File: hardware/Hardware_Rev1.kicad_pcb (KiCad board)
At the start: 2 copper layers, 101.6 x 50.8 mm, 52 parts, among them J1 RJ45_LED_Shielded, J2 6P6C, Q1 BUK7M33-60EX, Q2 BUK7M33-60EX, Q3 BUK7M33-60EX, U1 LT1910, U2 LT1910, U3 OKI, U4 LT1910, U5 TSR_1-2450, U6 Teensy4.1_DEV-16771

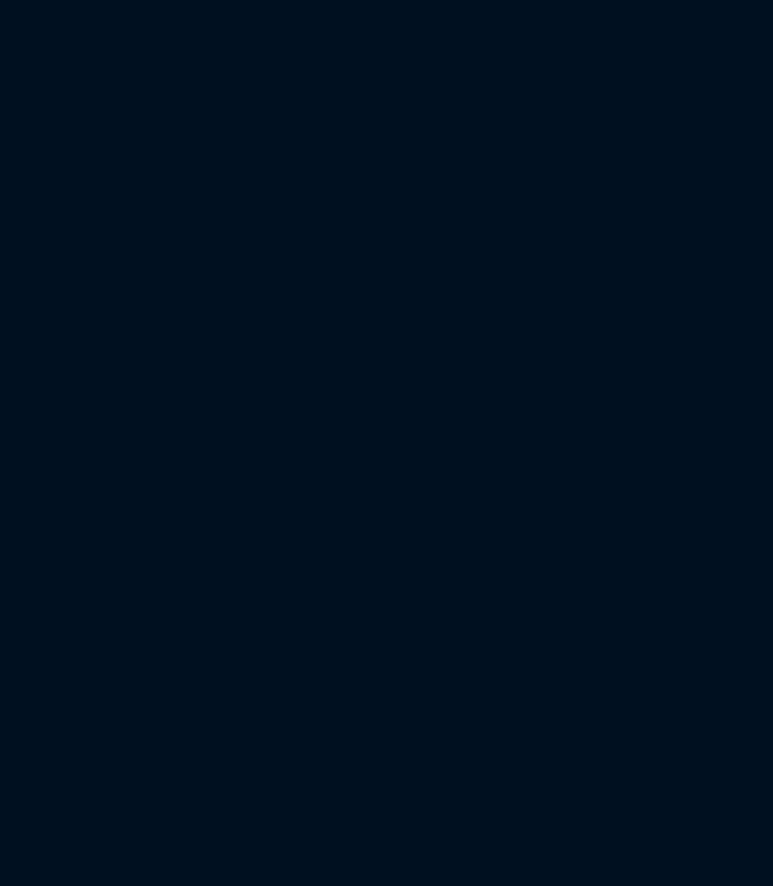
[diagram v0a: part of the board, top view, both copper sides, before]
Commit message: updated layout with drill holes (they don't fit??)
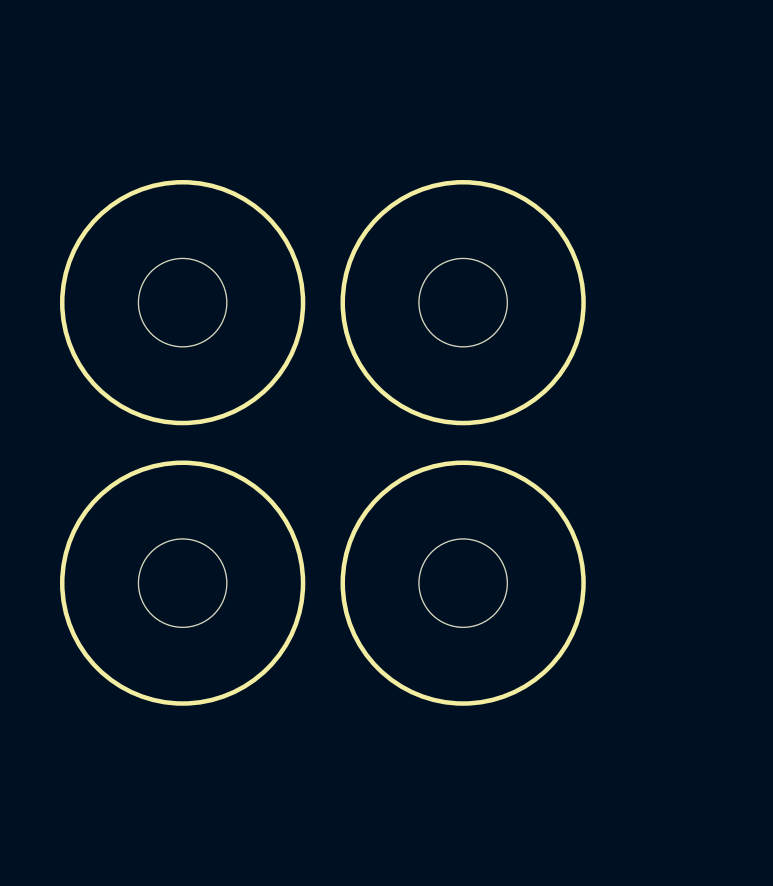
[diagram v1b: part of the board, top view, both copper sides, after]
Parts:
- added V1: Via, MRDT_Drill_Holes:4_40_Hole_Corner, F.Cu at (-342.9, -57.1)
- added V2: Via, MRDT_Drill_Holes:4_40_Hole_Corner, F.Cu at (-334.9, -66.5)
- added V3: Via, MRDT_Drill_Holes:4_40_Hole_Corner, F.Cu at (-333.6, -57.1)
- added V4: Via, MRDT_Drill_Holes:4_40_Hole_Corner, F.Cu at (-333.6, -66.5)
- Q1, Q2, Q3: value BUK7M33-60EX -> BUK9M9R5-40HX
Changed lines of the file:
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@@
     )
+  )
+  (footprint "MRDT_Drill_Holes:4_40_Hole_Corner" (layer "F.Cu")
+    (at -333.55 -57.15)
+    (property "Sheetfile" "Hardware_Rev1.kicad_sch")
+    (property "Sheetname" "")
+    (attr through_hole)
+    (fp_text reference "V3" (at 4.00812 -3.50812) (layer "F.SilkS") hide
+      (effects (font (size 1 1) (thickness 0.15)))
+    )
+    (fp_text value "Via" (at 4.00812 -4.50812) (layer "F.Fab") hide
+      (effects (font (size 1 1) (thickness 0.15)))
+    )
+    (fp_circle (center 4.00812 -4.00812) (end 4.00812 0.00508) (layer "F.SilkS") (width 0.15) (fill none))
+    (fp_line (start 4.0132 -8.0264) (end 0 -8.0264) (layer "F.Fab") (width 0.15))
+    (fp_line (start 0 0) (end 8.0264 0) (layer "F.Fab") (width 0.15))
+    (fp_line (start 8.0264 -4.0132) (end 8.0264 0) (layer "F.Fab") (width 0.15))
+    (fp_line (start 0 -8.0264) (end 0 0) (layer "F.Fab") (width 0.15))
+    (fp_arc (start 4.0132 -8.0264) (mid 6.850961 -6.850961) (end 8.0264 -4.0132) (layer "F.Fab") (width 0.15))
+    (pad "" np_thru_hole circle locked (at 4.00812 -4.00812) (size 2.9464 2.9464) (drill 2.9464) (layers *.Cu *.Mask)
+      (clearance 2.5))
   )
   (footprint "Capacitor_SMD:C_0603_1608Metric_Pad1.08x0.95mm_HandSolder" (layer "F.Cu")
@@
     )
   )
+  (footprint "MRDT_Drill_Holes:4_40_Hole_Corner" (layer "F.Cu")
+    (at -334.88376 -66.5 90)
+    (property "Sheetfile" "Hardware_Rev1.kicad_sch")
+    (property "Sheetname" "")
+    (attr through_hole)
+    (fp_text reference "V2" (at 4.00812 -3.50812 90) (layer "F.SilkS") hide
+      (effects (font (size 1 1) (thickness 0.15)))
+    )
+    (fp_text value "Via" (at 4.00812 -4.50812 90) (layer "F.Fab") hide
+      (effects (font (size 1 1) (thickness 0.15)))
+    )
+    (fp_circle (center 4.00812 -4.00812) (end 4.00812 0.00508) (layer "F.SilkS") (width 0.15) (fill none))
+    (fp_line (start 8.0264 -4.0132) (end 8.0264 0) (layer "F.Fab") (width 0.15))
+    (fp_line (start 0 0) (end 8.0264 0) (layer "F.Fab") (width 0.15))
+    (fp_line (start 4.0132 -8.0264) (end 0 -8.0264) (layer "F.Fab") (width 0.15))
+    (fp_line (start 0 -8.0264) (end 0 0) (layer "F.Fab") (width 0.15))
+    (fp_arc (start 4.0132 -8.0264) (mid 6.850961 -6.850961) (end 8.0264 -4.0132) (layer "F.Fab") (width 0.15))
+    (pad "" np_thru_hole circle locked (at 4.00812 -4.00812 90) (size 2.9464 2.9464) (drill 2.9464) (layers *.Cu *.Mask)
+      (clearance 2.5))
+  )
   (footprint "MRDT_Connectors:MOLEX_uF_S_03_Horizontal" (layer "F.Cu")
     (at -158.82 3.75 180)
@@
       (effects (font (size 1 1) (thickness 0.15)))
     )
-    (fp_text value "BUK7M33-60EX" (at 0 2.64) (layer "F.Fab")
+    (fp_text value "BUK9M9R5-40HX" (at 0 2.64) (layer "F.Fab")
       (effects (font (size 1 1) (thickness 0.15)))
     )
@@
       (effects (font (size 1 1) (thickness 0.15)))
     )
-    (fp_text value "BUK7M33-60EX" (at 0 2.64) (layer "F.Fab")
+    (fp_text value "BUK9M9R5-40HX" (at 0 2.64) (layer "F.Fab")
       (effects (font (size 1 1) (thickness 0.15)))
     )
@@
     )
   )
+  (footprint "MRDT_Drill_Holes:4_40_Hole_Corner" (layer "F.Cu")
+    (at -333.55 -66.5)
+    (property "Sheetfile" "Hardware_Rev1.kicad_sch")
+    (property "Sheetname" "")
+    (attr through_hole)
+    (fp_text reference "V4" (at 4.00812 -3.50812) (layer "F.SilkS") hide
+      (effects (font (size 1 1) (thickness 0.15)))
+    )
+    (fp_text value "Via" (at 4.00812 -4.50812) (layer "F.Fab") hide
+      (effects (font (size 1 1) (thickness 0.15)))
+    )
+    (fp_circle (center 4.00812 -4.00812) (end 4.00812 0.00508) (layer "F.SilkS") (width 0.15) (fill none))
+    (fp_line (start 0 0) (end 8.0264 0) (layer "F.Fab") (width 0.15))
+    (fp_line (start 4.0132 -8.0264) (end 0 -8.0264) (layer "F.Fab") (width 0.15))
+    (fp_line (start 8.0264 -4.0132) (end 8.0264 0) (layer "F.Fab") (width 0.15))
+    (fp_line (start 0 -8.0264) (end 0 0) (layer "F.Fab") (width 0.15))
+    (fp_arc (start 4.0132 -8.0264) (mid 6.850961 -6.850961) (end 8.0264 -4.0132) (layer "F.Fab") (width 0.15))
+    (pad "" np_thru_hole circle locked (at 4.00812 -4.00812) (size 2.9464 2.9464) (drill 2.9464) (layers *.Cu *.Mask)
+      (clearance 2.5))
+  )
   (footprint "Capacitor_SMD:C_0603_1608Metric_Pad1.08x0.95mm_HandSolder" (layer "F.Cu")
     (at -85.25 -60.59)
@@
       (effects (font (size 1 1) (thickness 0.15)))
     )
-    (fp_text value "BUK7M33-60EX" (at 0 2.64) (layer "F.Fab")
+    (fp_text value "BUK9M9R5-40HX" (at 0 2.64) (layer "F.Fab")
       (effects (font (size 1 1) (thickness 0.15)))
     )
@@
     )
   )
+  (footprint "MRDT_Drill_Holes:4_40_Hole_Corner" (layer "F.Cu")
+    (at -342.9 -57.15)
+    (property "Sheetfile" "Hardware_Rev1.kicad_sch")
+    (property "Sheetname" "")
+    (attr through_hole)
+    (fp_text reference "V1" (at 4.00812 -3.50812) (layer "F.SilkS") hide
+      (effects (font (size 1 1) (thickness 0.15)))
+    )
+    (fp_text value "Via" (at 4.00812 -4.50812) (layer "F.Fab") hide
+      (effects (font (size 1 1) (thickness 0.15)))
+    )
+    (fp_circle (center 4.00812 -4.00812) (end 4.00812 0.00508) (layer "F.SilkS") (width 0.15) (fill none))
+    (fp_line (start 0 -8.0264) (end 0 0) (layer "F.Fab") (width 0.15))
+    (fp_line (start 4.0132 -8.0264) (end 0 -8.0264) (layer "F.Fab") (width 0.15))
+    (fp_line (start 8.0264 -4.0132) (end 8.0264 0) (layer "F.Fab") (width 0.15))
+    (fp_line (start 0 0) (end 8.0264 0) (layer "F.Fab") (width 0.15))
+    (fp_arc (start 4.0132 -8.0264) (mid 6.850961 -6.850961) (end 8.0264 -4.0132) (layer "F.Fab") (width 0.15))
+    (pad "" np_thru_hole circle locked (at 4.00812 -4.00812) (size 2.9464 2.9464) (drill 2.9464) (layers *.Cu *.Mask)
+      (clearance 2.5))
+  )
   (footprint "Package_SO:SOIC-8-N7_3.9x4.9mm_P1.27mm" (layer "F.Cu")

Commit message: Worked on Layout of Drivers and Bucks
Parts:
- moved D5 202.3 mm to (-311.2, -89.5)
- moved C3 199.4 mm to (-287.3, -105.7)
- moved R8 194.9 mm to (-307.0, -91.5), turned to -90 degrees
- moved V3 194.6 mm to (-142.8, -18.5)
- moved V4 194.6 mm to (-142.8, -27.9)
- moved V1 194.6 mm to (-152.2, -18.5)
- moved V2 194.6 mm to (-144.1, -27.9)
- moved D4 161.2 mm to (-287.3, -113.7)
- moved C6 158.4 mm to (-282.2, -105.7), turned to 180 degrees
- moved C7 155.8 mm to (-282.2, -109.0), turned to 180 degrees
- moved R6 155.3 mm to (-282.0, -115.1)
- moved D2 146.7 mm to (-262.9, -97.9)
- moved R4 142.8 mm to (-257.2, -93.0), turned to 90 degrees
- moved C4 141.9 mm to (-262.5, -94.7)
- moved Q1 141.3 mm to (-253.1, -89.2)
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
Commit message: Fixed up tracings, starting to put everything together.
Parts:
- Conn1: moved to B.Cu
- moved U6 442.5 mm to (126.7, 28.7)
- moved C1 425.0 mm to (75.3, 157.8)
- moved C10 425.0 mm to (156.7, 155.8)
- moved C2 425.0 mm to (110.9, 160.2)
- moved C3 425.0 mm to (57.5, 142.8)
- moved C4 425.0 mm to (82.3, 153.8)
- moved C5 425.0 mm to (118.7, 156.4)
- moved C6 425.0 mm to (62.5, 142.8)
- moved C7 425.0 mm to (62.5, 139.5)
- moved C8 425.0 mm to (149.5, 158.3)
- moved Conn10 425.0 mm to (157.4, 142.2)
- moved Conn4 425.0 mm to (92.0, 135.4)
- moved Conn5 425.0 mm to (92.0, 145.1)
- moved Conn6 425.0 mm to (123.4, 132.8)
- moved Conn7 425.0 mm to (122.6, 143.9)
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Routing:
- added copper zone on B.Cu, net (none)
- added copper zone on F.Cu, net GND
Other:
- board size 101.6 x 50.8 mm -> 131.1 x 65.8 mm

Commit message: closing kicad
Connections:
- C10 pad 1: +12VA -> +12V
- C4 pad 1: +12VA -> +12V
- C5 pad 1: +12VA -> +12V
- Q1 pad 5: +12VA -> +12V
- Q2 pad 5: +12VA -> +12V
- Q3 pad 5: +12VA -> +12V
- R3 pad 1: +12VA -> +12V
- U1 pad 6: +12VA -> +12V
- U1 pad 8: +12VA -> +12V
- U2 pad 6: +12VA -> +12V
- U2 pad 8: +12VA -> +12V
- U4 pad 6: +12VA -> +12V
- U4 pad 8: +12VA -> +12V

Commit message: only drive circuit placement left
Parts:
- Conn2, Conn3, Conn8: moved to B.Cu
- moved U6 147.2 mm to (237.5, 125.7), turned to 180 degrees
- moved Conn9 124.6 mm to (194.1, 12.8)
- moved Conn4 123.7 mm to (134.9, 19.3)
- moved Conn5 123.7 mm to (134.8, 29.0)
- moved Conn10 123.5 mm to (194.3, 24.4)
- moved Conn7 122.3 mm to (164.1, 28.9)
- moved Conn6 122.3 mm to (164.8, 17.8)
- moved D5 111.5 mm to (106.1, 74.2)
- moved R8 109.8 mm to (109.7, 74.2), turned to 180 degrees
- moved U5 105.6 mm to (117.7, 88.5), turned to 180 degrees
- moved C3 88.9 mm to (109.7, 70.9), turned to 180 degrees
- moved C5 84.4 mm to (109.7, 72.4)
- moved U3 74.9 mm to (100.6, 87.6)
- moved Conn2 74.6 mm to (202.9, 107.7), turned to 0 degrees
- moved Conn8 72.9 mm to (186.9, 107.7), turned to 0 degrees
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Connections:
- Conn1 pad 2: (no net) -> +12V

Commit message: placed everything
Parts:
- Conn10, Conn4, Conn5, Conn6, Conn7, Conn9: moved to B.Cu
- moved D1 114.0 mm to (106.0, 72.6)
- moved R1 110.5 mm to (140.2, 71.5), turned to 180 degrees
- moved C1 106.8 mm to (140.2, 73.0), turned to 0 degrees
- moved R2 106.2 mm to (165.6, 71.6), turned to 180 degrees
- moved C2 102.7 mm to (165.5, 73.2), turned to 0 degrees
- moved U1 101.4 mm to (134.1, 72.4), turned to 180 degrees
- moved R7 98.5 mm to (191.0, 71.6), turned to 180 degrees
- moved U2 98.4 mm to (159.8, 72.4), turned to 180 degrees
- moved R3 97.9 mm to (109.7, 72.6), turned to 180 degrees
- moved C8 94.7 mm to (191.0, 73.2), turned to 0 degrees
- moved Q2 93.9 mm to (148.9, 71.6), turned to 180 degrees
- moved Q1 93.8 mm to (124.8, 71.6), turned to 180 degrees
- moved U4 92.2 mm to (184.9, 72.4), turned to 180 degrees
- moved C4 91.6 mm to (128.8, 75.4), turned to -90 degrees
- moved D2 90.9 mm to (136.0, 77.5), turned to 180 degrees
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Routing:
- net Heater2: track 0.00 -> 5.56 mm
- net Heater3: track 0.00 -> 5.55 mm
- net Heater1: track 0.00 -> 5.05 mm

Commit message: started tracing
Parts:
- moved C5 69.2 mm to (177.0, 53.6), turned to -90 degrees
- moved Conn3 50.9 mm to (188.5, 59.7), turned to 180 degrees
- moved Conn8 50.6 mm to (203.2, 59.7), turned to 180 degrees
- moved Conn2 41.6 mm to (210.5, 66.8), turned to 90 degrees
- moved D6 36.5 mm to (153.8, 60.7)
- moved R9 36.4 mm to (150.4, 60.7)
- moved C8 35.1 mm to (158.0, 61.3), turned to -90 degrees
- moved R7 33.2 mm to (159.5, 61.2), turned to 90 degrees
- moved Q3 32.5 mm to (147.8, 54.1), turned to 90 degrees
- moved Conn10 32.0 mm to (143.5, 59.7)
- moved C10 31.9 mm to (155.2, 53.6)
- moved Conn9 31.2 mm to (152.1, 59.7)
- moved U4 31.1 mm to (158.8, 55.6), turned to 90 degrees
- moved Q2 27.5 mm to (169.7, 53.5), turned to 90 degrees
- moved U2 26.9 mm to (180.6, 55.4), turned to 90 degrees
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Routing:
- net Net-(C13-Pad2): track 0.00 -> 35.3 mm, vias 0 -> 2
- net Net-(J1-Pad10): track 0.00 -> 27.9 mm
- net Net-(C13-Pad1): track 0.00 -> 18.9 mm
- net +3V3: track 0.00 -> 16.4 mm
- net Net-(Q1-Pad4): track 0.00 -> 16.4 mm, vias 0 -> 2
- net Net-(J1-Pad3): track 0.00 -> 13.6 mm
- net +12V: track 0.00 -> 10.9 mm
- net Net-(J1-Pad1): track 0.00 -> 6.22 mm
- net Net-(J1-Pad4): track 0.00 -> 5.60 mm
- net Net-(J1-Pad6): track 0.00 -> 5.40 mm, vias 0 -> 2
- net Heater2: track 5.56 -> 2.76 mm
- net Heater3: track 5.55 -> 3.02 mm
- net Net-(C8-Pad1): track 0.00 -> 2.18 mm
- net Net-(C1-Pad1): track 0.00 -> 2.08 mm
- net Net-(C2-Pad1): track 0.00 -> 2.08 mm
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- added copper zone on F.Cu, net +12V
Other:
- board size 131.1 x 65.8 mm -> 131.1 x 50.4 mm
- board text added: "Heater 1"
- board text added: "Heater 2"
- board text added: "Heater 3"

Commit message: added name stuff
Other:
- board text added: "Water Heater Board 2022 - Rev 1 Jacob Byers, James Elverson, Joshua Perkins #ROVESOHARD"
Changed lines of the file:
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@@
+    (effects (font (size 1.5 1.5) (thickness 0.3)))
+  )
+  (gr_text "Water Heater Board 2022 - Rev 1\nJacob Byers, James Elverson, Joshua Perkins\n#ROVESOHARD" (at 183.134 95.504) (layer "F.Cu")
     (effects (font (size 1.5 1.5) (thickness 0.3)))
   )
